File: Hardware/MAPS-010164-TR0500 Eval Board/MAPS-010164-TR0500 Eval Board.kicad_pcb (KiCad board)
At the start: 2 copper layers, 48.5 x 38.8 mm, 13 parts, among them IC1 MAPS-010164-TR0500, J1 Conn_Coaxial, J2 Conn_Coaxial, J3 Conn_02x02_Top_Bottom, J4 Conn_02x02_Top_Bottom, J5 Conn_02x04_Top_Bottom, J6 Conn_Coaxial, J7 Conn_Coaxial, J8 Conn_02x02_Top_Bottom

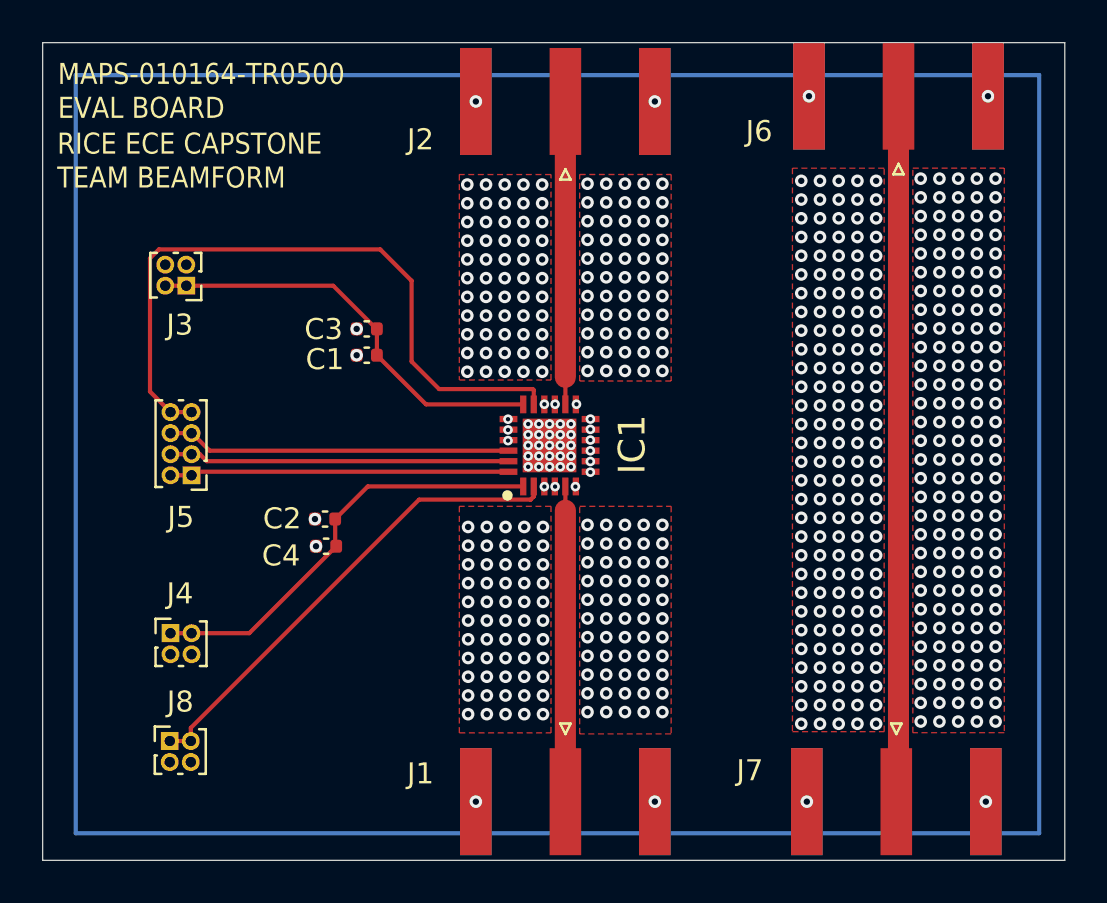
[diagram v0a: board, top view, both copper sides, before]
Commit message: Digital Line Filtering
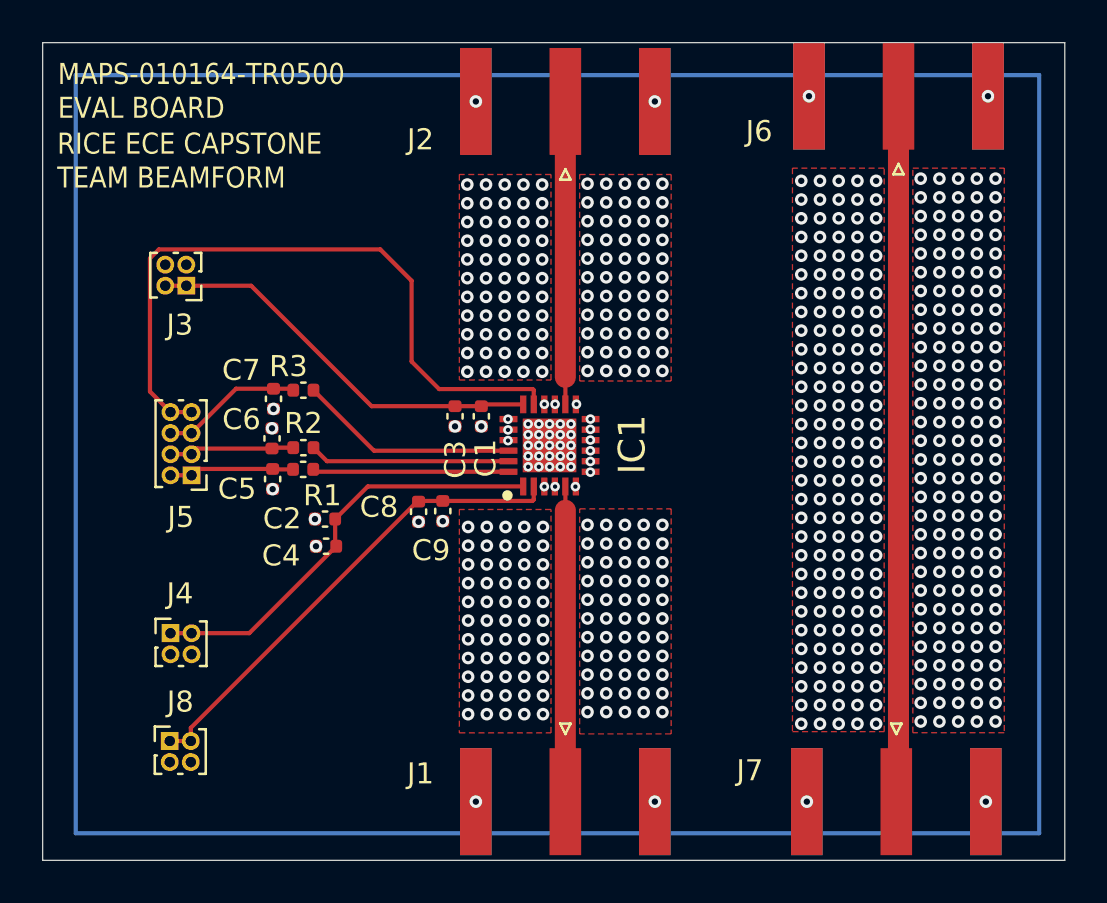
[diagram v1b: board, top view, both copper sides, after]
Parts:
- added C5: 300 pF, Capacitor_SMD:C_0402_1005Metric, F.Cu at (92.1, 62.4)
- added C6: 300 pF, Capacitor_SMD:C_0402_1005Metric, F.Cu at (92.1, 60.5)
- added C7: 300 pF, Capacitor_SMD:C_0402_1005Metric, F.Cu at (92.1, 58.6)
- added C8: 0.1uF, Capacitor_SMD:C_0402_1005Metric, F.Cu at (99.0, 64.0)
- added C9: 100p, Capacitor_SMD:C_0402_1005Metric, F.Cu at (100.2, 64.0)
- added R1: 10, Capacitor_SMD:C_0402_1005Metric, F.Cu at (93.5, 62.0)
- added R2: 10, Capacitor_SMD:C_0402_1005Metric, F.Cu at (93.6, 60.9)
- added R3: 10, Capacitor_SMD:C_0402_1005Metric, F.Cu at (93.6, 58.2)
- moved C1 6.16 mm to (102.0, 59.5), turned to 90 degrees
- moved C3 5.90 mm to (100.8, 59.5), turned to 90 degrees
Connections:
- IC1 pad 22: LE -> Net-(IC1-D3_OR_LE)
- IC1 pad 23: CLK -> Net-(IC1-D2_OR_CLK)
- IC1 pad 24: SER IN -> Net-(IC1-D1_OR_SER_IN)
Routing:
- net Net-(IC1-D3_OR_LE): track 0.00 -> 10.5 mm
- net CLK: track 16.2 -> 5.96 mm
- net SER IN: track 16.1 -> 5.95 mm
- net LE: track 16.4 -> 6.76 mm
- net Net-(IC1-D2_OR_CLK): track 0.00 -> 9.53 mm
- net Net-(IC1-D1_OR_SER_IN): track 0.00 -> 9.32 mm
- net Vcc: track 43.0 -> 42.4 mm
- net GND: vias 572 -> 577

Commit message: Attenuator board. TODO: Waveguides
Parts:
- added C10: 300 pF, Capacitor_SMD:C_0402_1005Metric, F.Cu at (95.5, 51.7)
- added R4: 10, Capacitor_SMD:C_0402_1005Metric, F.Cu at (94.0, 51.3)
- moved R3 2.61 mm to (91.0, 58.1)
- moved C6 1.97 mm to (94.0, 60.5)
- moved C5 1.29 mm to (93.0, 63.4)
- moved R1 1.03 mm to (92.5, 61.9)
- moved R2 0.94 mm to (92.6, 60.9)
- moved C7 0.20 mm to (92.3, 58.6)
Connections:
- C5 pad 1: SER IN -> Net-(IC1-D1_OR_SER_IN)
- C6 pad 1: CLK -> Net-(IC1-D2_OR_CLK)
- C7 pad 1: LE -> Net-(IC1-D3_OR_LE)
- IC1 pad 17: SER OUT -> Net-(IC1-SER_OUT)
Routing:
- net SER OUT: track 32.8 -> 16.3 mm
- net Net-(IC1-SER_OUT): track 0.00 -> 15.8 mm
- net LE: track 6.76 -> 4.01 mm
- net Net-(IC1-D3_OR_LE): track 10.5 -> 13.1 mm
- net Net-(IC1-D1_OR_SER_IN): track 9.32 -> 11.3 mm
- net CLK: track 5.96 -> 4.93 mm
- net SER IN: track 5.95 -> 4.97 mm
- net Net-(IC1-D2_OR_CLK): track 9.53 -> 10.5 mm
- net GND: vias 577 -> 578

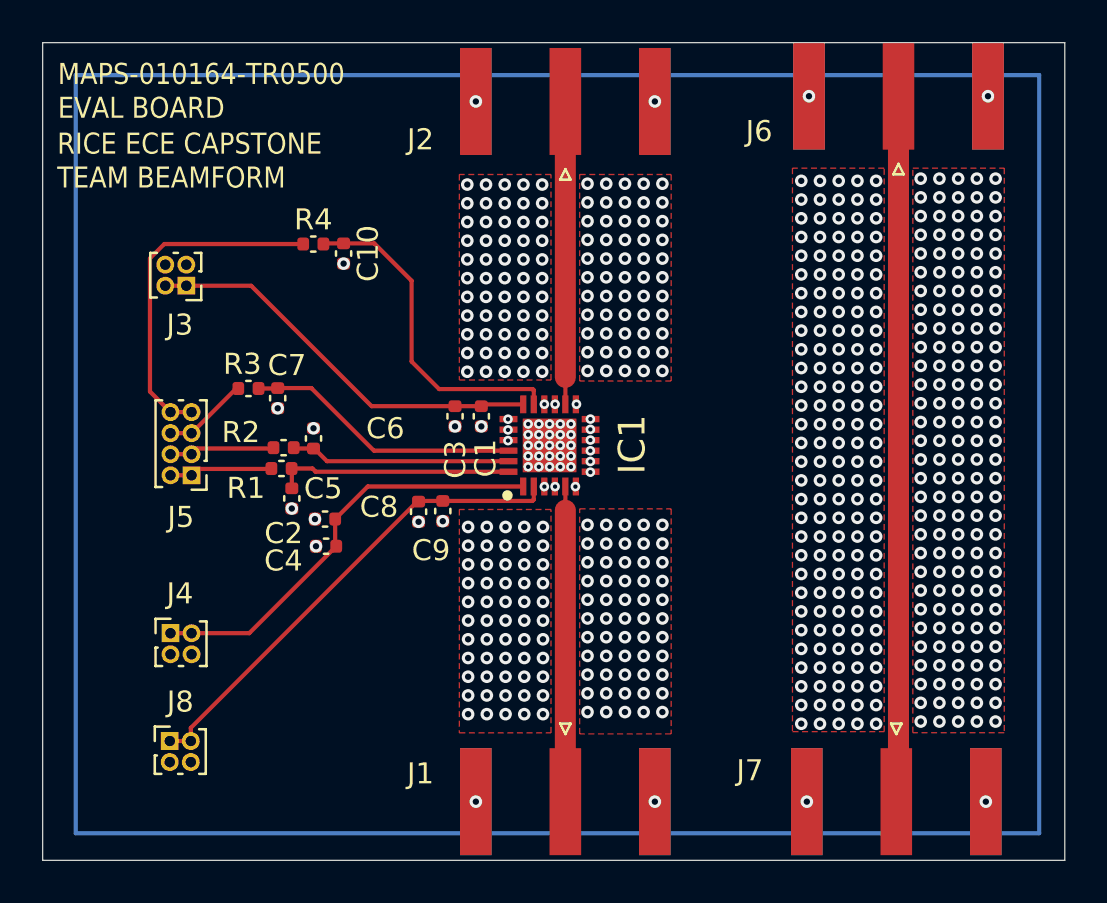
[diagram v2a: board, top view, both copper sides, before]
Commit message: DRC and header re-sizing
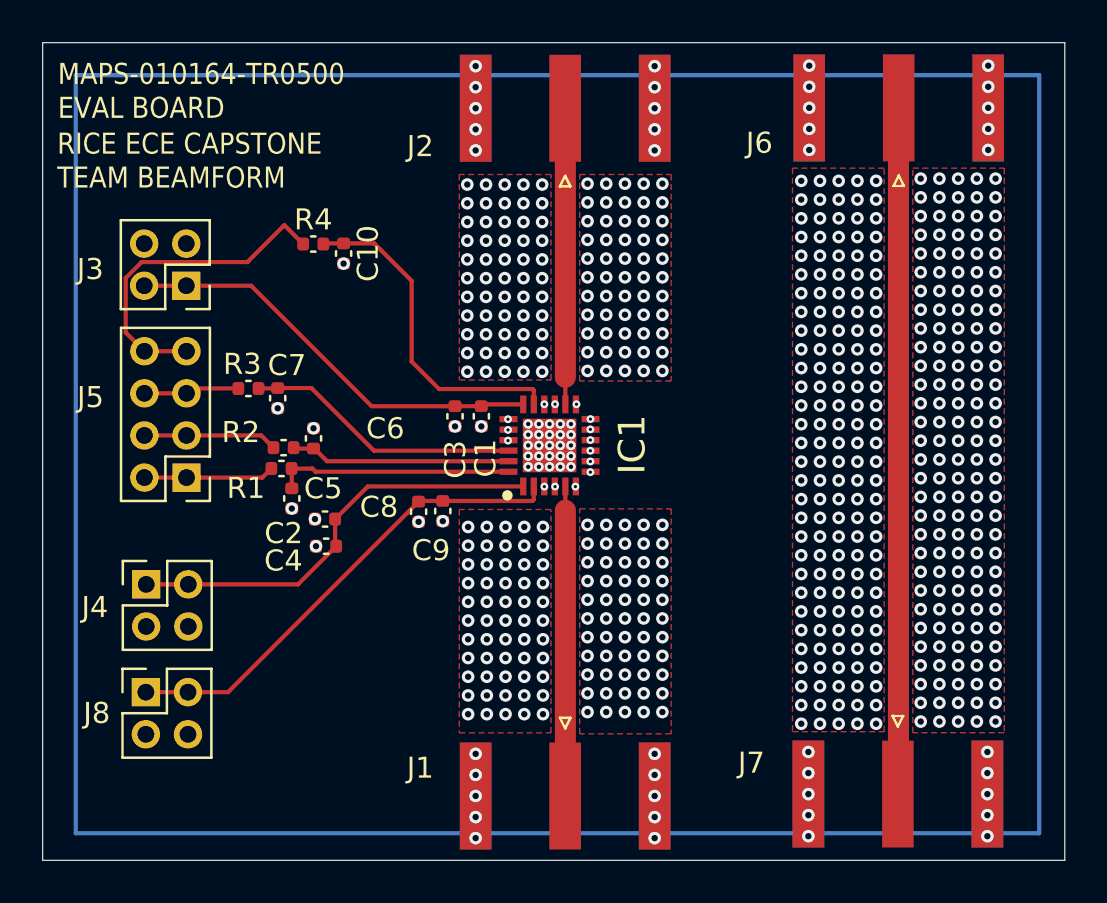
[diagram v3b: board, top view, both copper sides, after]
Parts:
- J3, J4, J8: footprint Connector_PinHeader_1.00mm:PinHeader_2x02_P1.00mm_Vertical -> Connector_PinHeader_2.00mm:PinHeader_2x02_P2.00mm_Vertical
- J5: footprint Connector_PinHeader_1.00mm:PinHeader_2x04_P1.00mm_Vertical -> Connector_PinHeader_2.00mm:PinHeader_2x04_P2.00mm_Vertical
- moved J4 2.59 mm to (86.1, 67.4)
- moved J8 2.58 mm to (86.1, 72.5)
- moved J6 0.55 mm to (121.8, 44.8)
- moved J7 0.37 mm to (121.8, 77.4)
- moved J2 0.32 mm to (106.0, 44.8)
- moved J1 0.27 mm to (106.0, 77.5)
- moved J5 0.26 mm to (88.0, 62.4)
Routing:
- net SER IN: track 4.97 -> 6.63 mm
- net CLK: track 4.93 -> 6.40 mm
- net Vcc: track 42.4 -> 43.3 mm
- net SER OUT: track 16.3 -> 15.7 mm
- net LE: track 4.01 -> 4.56 mm
- net GND: vias 578 -> 610

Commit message: Fixed JLCPCB Errors
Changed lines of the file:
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@@
 			(plot_on_all_layers_selection 0x00000000_00000000_00000000_00000000)
 			(disableapertmacros no)
-			(usegerberextensions no)
+			(usegerberextensions yes)
 			(usegerberattributes yes)
 			(usegerberadvancedattributes yes)
@@
 			(sketchdnponfab yes)
 			(crossoutdnponfab yes)
-			(subtractmaskfromsilk no)
+			(subtractmaskfromsilk yes)
 			(outputformat 1)
 			(mirror no)
-			(drillshape 1)
+			(drillshape 0)
 			(scaleselection 1)
-			(outputdirectory "")
+			(outputdirectory "MAPS-010164-TR500-EVAL-GRB/")
 		)
 	)
@@
 	(via
 		(at 106.5276 58.8772)
-		(size 0.375)
-		(drill 0.15)
+		(size 0.45)
+		(drill 0.2)
 		(layers "F.Cu" "B.Cu")
 		(net 1)
@@
 	)
 	(via
+		(at 103.11 59.58)
+		(size 0.45)
+		(drill 0.2)
+		(layers "F.Cu" "B.Cu")
+		(net 1)
+	)
+	(via
 		(at 117.202 59.8265)
 		(size 0.6)
@@
 	)
 	(via
+		(at 105.49 62.98)
+		(size 0.45)
+		(drill 0.2)
+		(layers "F.Cu" "B.Cu")
+		(net 1)
+	)
+	(via
 		(at 101.74 46.8225)
 		(size 0.6)
@@
 	)
 	(via
-		(at 107.188 61.087)
-		(size 0.375)
-		(drill 0.15)
-		(layers "F.Cu" "B.Cu")
-		(net 1)
-	)
-	(via
 		(at 119.869 48.2695)
 		(size 0.6)
@@
 	)
 	(via
+		(at 103.5 60.1)
+		(size 0.45)
+		(drill 0.2)
+		(layers "F.Cu" "B.Cu")
+		(net 1)
+	)
+	(via
 		(at 122.874 61.5)
 		(size 0.6)
@@
 	)
 	(via
-		(at 105.5116 62.7888)
-		(size 0.375)
-		(drill 0.15)
-		(layers "F.Cu" "B.Cu")
-		(net 1)
-	)
-	(via
 		(at 118.091 49.1585)
 		(size 0.6)
@@
 	)
 	(via
+		(at 106.5 62.82)
+		(size 0.45)
+		(drill 0.2)
+		(layers "F.Cu" "B.Cu")
+		(net 1)
+	)
+	(via
 		(at 104.01 51.112)
 		(size 0.6)
@@
 	)
 	(via
-		(at 103.2764 59.5884)
-		(size 0.375)
-		(drill 0.15)
-		(layers "F.Cu" "B.Cu")
-		(net 1)
-	)
-	(via
 		(at 107.052 72.606)
 		(size 0.6)
@@
 	)
 	(via
+		(at 105 62.58)
+		(size 0.45)
+		(drill 0.2)
+		(layers "F.Cu" "B.Cu")
+		(net 1)
+	)
+	(via
 		(at 118.091 52.7145)
 		(size 0.6)
@@
 	)
 	(via
+		(at 104.98 59.08)
+		(size 0.45)
+		(drill 0.2)
+		(layers "F.Cu" "B.Cu")
+		(net 1)
+	)
+	(via
 		(at 104.01 57.335)
 		(size 0.6)
@@
 	)
 	(via
-		(at 107.188 61.595)
-		(size 0.375)
-		(drill 0.15)
-		(layers "F.Cu" "B.Cu")
-		(net 1)
-	)
-	(via
 		(at 107.941 66.383)
 		(size 0.6)
@@
 	)
 	(via
-		(at 105.0036 62.7888)
-		(size 0.375)
-		(drill 0.15)
-		(layers "F.Cu" "B.Cu")
-		(net 1)
-	)
-	(via
 		(at 126.43 62.389)
 		(size 0.6)
@@
 	)
 	(via
-		(at 103.2764 60.6044)
-		(size 0.375)
-		(drill 0.15)
-		(layers "F.Cu" "B.Cu")
-		(net 1)
-	)
-	(via
 		(at 109.719 67.272)
 		(size 0.6)
@@
 	)
 	(via
+		(at 107.41 60.58)
+		(size 0.45)
+		(drill 0.2)
+		(layers "F.Cu" "B.Cu")
+		(net 1)
+	)
+	(via
 		(at 100.76 59.9302)
 		(size 0.6)
@@
 	)
 	(via
-		(at 103.2764 60.0964)
-		(size 0.375)
-		(drill 0.15)
-		(layers "F.Cu" "B.Cu")
-		(net 1)
-	)
-	(via
 		(at 101.382 65.594)
 		(size 0.6)
@@
 	)
 	(via
+		(at 105.51 58.68)
+		(size 0.45)
+		(drill 0.2)
+		(layers "F.Cu" "B.Cu")
+		(net 1)
+	)
+	(via
 		(at 101.74 75.48)
 		(size 0.6)
@@
 	)
 	(via
-		(at 107.188 60.579)
-		(size 0.375)
-		(drill 0.15)
-		(layers "F.Cu" "B.Cu")
-		(net 1)
-	)
-	(via
 		(at 119.869 67.8275)
 		(size 0.6)
@@
 	)
 	(via
-		(at 107.188 62.103)
-		(size 0.375)
-		(drill 0.15)
-		(layers "F.Cu" "B.Cu")
-		(net 1)
-	)
-	(via
 		(at 126.08 44.8025)
 		(size 0.6)
@@
 	)
 	(via
-		(at 107.188 60.071)
-		(size 0.375)
-		(drill 0.15)
-		(layers "F.Cu" "B.Cu")
-		(net 1)
-	)
-	(via
 		(at 104.938 67.372)
 		(size 0.6)
@@
 	)
 	(via
-		(at 107.19 59.583)
-		(size 0.375)
-		(drill 0.15)
-		(layers "F.Cu" "B.Cu")
-		(net 1)
-	)
-	(via
 		(at 107.941 48.405)
 		(size 0.6)
@@
 	)
 	(via
+		(at 106.98 62.09)
+		(size 0.45)
+		(drill 0.2)
+		(layers "F.Cu" "B.Cu")
+		(net 1)
+	)
+	(via
+		(at 107 60.08)
+		(size 0.45)
+		(drill 0.2)
+		(layers "F.Cu" "B.Cu")
+		(net 1)
+	)
+	(via
 		(at 119.869 50.0475)
 		(size 0.6)
@@
 	)
 	(via
+		(at 106.99 61.08)
+		(size 0.45)
+		(drill 0.2)
+		(layers "F.Cu" "B.Cu")
+		(net 1)
+	)
+	(via
 		(at 99.03 64.46)
 		(size 0.6)
@@
 	)
 	(via
-		(at 106.4768 62.7888)
-		(size 0.375)
-		(drill 0.15)
-		(layers "F.Cu" "B.Cu")
-		(net 1)
-	)
-	(via
 		(at 120.758 48.2695)
 		(size 0.6)
@@
 	)
 	(via
+		(at 107.4 59.59)
+		(size 0.45)
+		(drill 0.2)
+		(layers "F.Cu" "B.Cu")
+		(net 1)
+	)
+	(via
 		(at 119.869 64.2715)
 		(size 0.6)
@@
 	)
 	(via
-		(at 105.5116 58.8772)
-		(size 0.375)
-		(drill 0.15)
-		(layers "F.Cu" "B.Cu")
-		(net 1)
-	)
-	(via
 		(at 108.83 57.295)
 		(size 0.6)
@@
 	)
 	(via
-		(at 105.0036 58.8772)
-		(size 0.375)
-		(drill 0.15)
-		(layers "F.Cu" "B.Cu")
-		(net 1)
-	)
-	(via
 		(at 110.24 45.8225)
 		(size 0.6)
@@
 	)
 	(via
+		(at 103.1 60.59)
+		(size 0.45)
+		(drill 0.2)
+		(layers "F.Cu" "B.Cu")
+		(net 1)
+	)
+	(via
 		(at 105.25 59.817)
 		(size 0.4572)
@@
 		(layers "F.Cu" "B.Cu")
 		(net 1)
+	)
+	(via
+		(at 107.4 61.6)
+		(size 0.45)
+		(drill 0.2)
+		(layers "F.Cu" "B.Cu")
+		(net 1)
